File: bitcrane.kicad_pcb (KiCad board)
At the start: 4 copper layers, 110 x 100 mm, 87 parts, among them J1 PSU Comm, J14 0353180420, J15 0353180420, J16 0353180420, J17 0353180420, J2 Hashboard0, J3 0455580003, J4 61900411021, J5 61900411021, J6 61900411021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

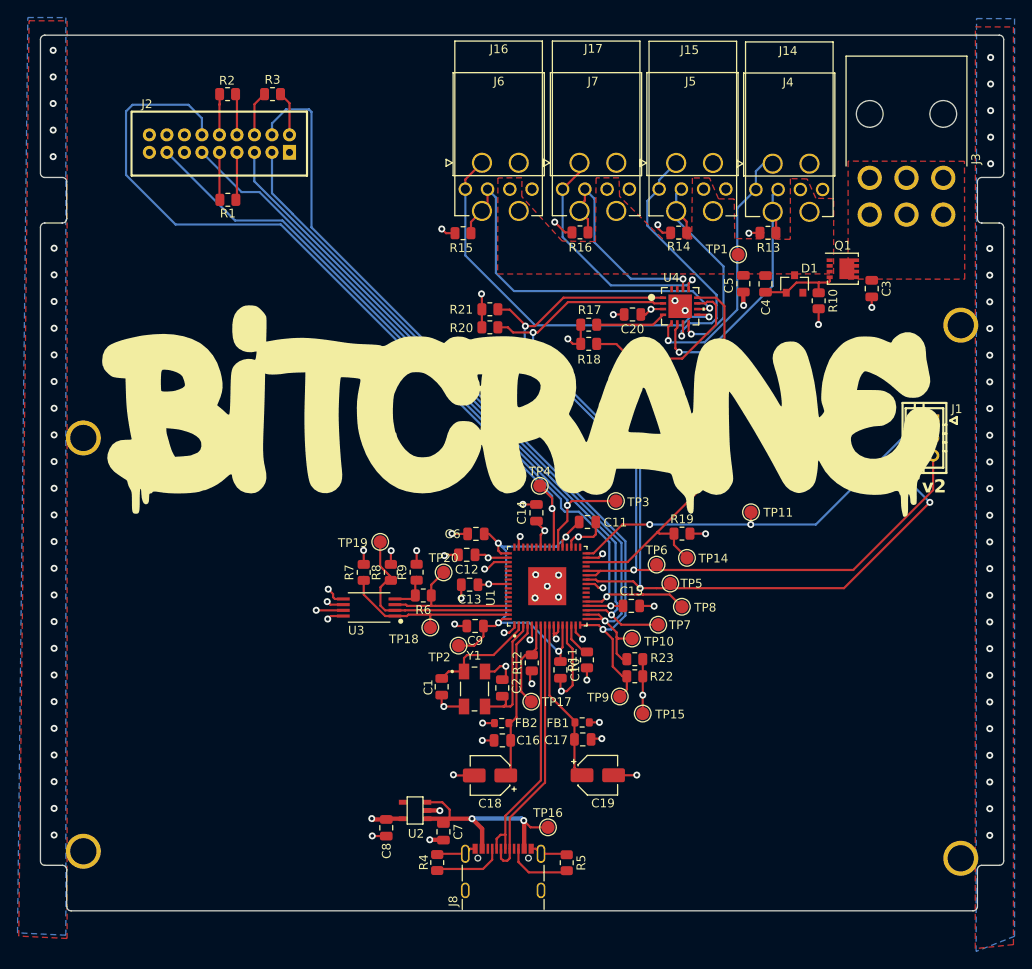
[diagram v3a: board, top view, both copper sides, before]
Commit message: switched to 3 HB connectors. added I2C hub. routed
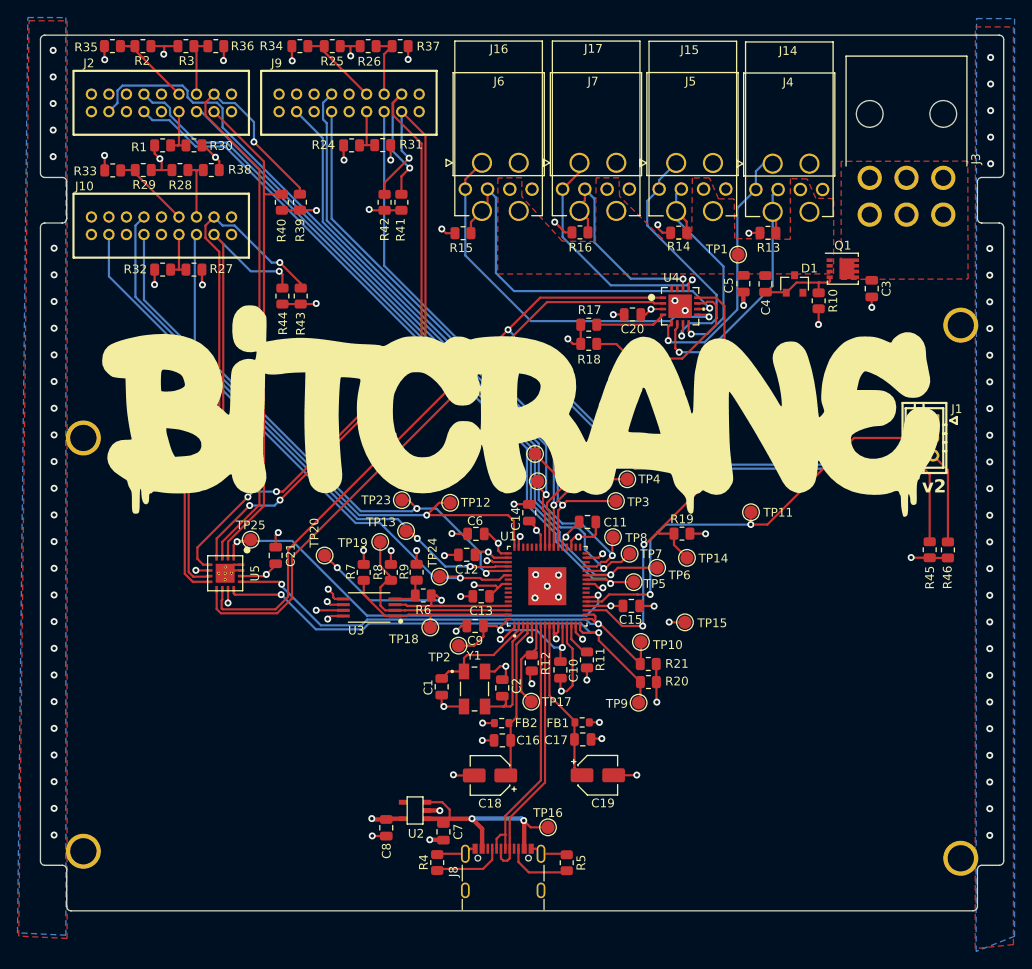
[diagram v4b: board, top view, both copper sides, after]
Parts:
- removed R22, R23: 4.7K, Resistor_SMD:R_0805_2012Metric
- added C21: 0.1uF, Capacitor_SMD:C_0805_2012Metric, F.Cu at (85.1, 93.7)
- added J10: Hashboard2, bitcart:CONN-TH_X2026WV-2-09D-46SN, F.Cu at (72.1, 56.0)
- added J9: Hashboard1, bitcart:CONN-TH_X2026WV-2-09D-46SN, F.Cu at (93.5, 42.0)
- added R24: 4.7K, Resistor_SMD:R_0805_2012Metric, F.Cu at (93.8, 46.8)
- added R25: 4.7K, Resistor_SMD:R_0805_2012Metric, F.Cu at (91.6, 35.5)
- added R26: 4.7K, Resistor_SMD:R_0805_2012Metric, F.Cu at (95.7, 35.5)
- added R27: 4.7K, Resistor_SMD:R_0805_2012Metric, F.Cu at (75.8, 61.0)
- added R28: 4.7K, Resistor_SMD:R_0805_2012Metric, F.Cu at (70.0, 49.6)
- added R29: 4.7K, Resistor_SMD:R_0805_2012Metric, F.Cu at (74.2, 49.6)
- added R30: 4.7K, Resistor_SMD:R_0805_2012Metric, F.Cu at (75.8, 46.8)
- added R31: 4.7K, Resistor_SMD:R_0805_2012Metric, F.Cu at (97.3, 46.8)
- added R32: 4.7K, Resistor_SMD:R_0805_2012Metric, F.Cu at (72.2, 61.0)
- added R33: 4.7K, Resistor_SMD:R_0805_2012Metric, F.Cu at (66.5, 49.7)
- added R34: 4.7K, Resistor_SMD:R_0805_2012Metric, F.Cu at (87.9, 35.5)
- added R35: 4.7K, Resistor_SMD:R_0805_2012Metric, F.Cu at (66.5, 35.5)
- added R36: 4.7K, Resistor_SMD:R_0805_2012Metric, F.Cu at (78.3, 35.5)
- added R37: 4.7K, Resistor_SMD:R_0805_2012Metric, F.Cu at (99.3, 35.5)
- added R38: 4.7K, Resistor_SMD:R_0805_2012Metric, F.Cu at (77.8, 49.6)
- added R39: 4.7K, Resistor_SMD:R_0805_2012Metric, F.Cu at (87.9, 53.3)
- added R40: 4.7K, Resistor_SMD:R_0805_2012Metric, F.Cu at (85.8, 53.3)
- added R41: 4.7K, Resistor_SMD:R_0805_2012Metric, F.Cu at (99.5, 53.3)
- added R42: 4.7K, Resistor_SMD:R_0805_2012Metric, F.Cu at (97.6, 53.3)
- added R43: 4.7K, Resistor_SMD:R_0805_2012Metric, F.Cu at (88.0, 64.0)
- added R44: 4.7K, Resistor_SMD:R_0805_2012Metric, F.Cu at (85.9, 64.0)
- added R45: 4.7K, Resistor_SMD:R_0805_2012Metric, F.Cu at (159.8, 93.0)
- added R46: 4.7K, Resistor_SMD:R_0805_2012Metric, F.Cu at (161.9, 93.0)
- added TP12: TestPoint, TestPoint:TestPoint_Pad_D1.5mm, F.Cu at (105.0, 87.7)
- added TP13: TestPoint, TestPoint:TestPoint_Pad_D1.5mm, F.Cu at (100.0, 90.9)
- added TP21: TestPoint, TestPoint:TestPoint_Pad_D1.5mm, F.Cu at (114.7, 82.1)
- added TP22: TestPoint, TestPoint:TestPoint_Pad_D1.5mm, F.Cu at (115.0, 85.2)
- added TP23: TestPoint, TestPoint:TestPoint_Pad_D1.5mm, F.Cu at (99.5, 87.3)
- added TP24: TestPoint, TestPoint:TestPoint_Pad_D1.5mm, F.Cu at (103.8, 96.1)
- added TP25: TestPoint, TestPoint:TestPoint_Pad_D1.5mm, F.Cu at (82.3, 91.9)
- added U5: PCA9546ARGVR, bitcart:QFN-16_EP_4x4_Pitch0.65mm, F.Cu at (79.4, 95.7)
- moved R20 44.4 mm to (127.7, 108.1), turned to 0 degrees
- moved R21 44.4 mm to (127.7, 106.1), turned to 0 degrees
- moved TP20 13.7 mm to (90.7, 93.7)
- moved TP15 11.5 mm to (131.9, 101.3)
- moved R3 11.3 mm to (74.9, 35.5), turned to 180 degrees
- moved TP8 11.2 mm to (123.7, 91.6)
- moved R2 11.1 mm to (70.0, 35.5), turned to 0 degrees
- moved TP4 10.0 mm to (125.3, 85.0)
- moved R1 9.71 mm to (72.2, 46.8)
- moved TP7 8.74 mm to (125.5, 93.5)
- moved J2 8.10 mm to (72.1, 42.0)
- moved TP5 4.18 mm to (126.0, 96.7)
- moved TP9 2.26 mm to (126.6, 110.5)
- moved C13 1.87 mm to (108.6, 98.3)
- moved TP10 1.08 mm to (126.8, 103.5)
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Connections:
- net /A0 renamed /A00
- net /A1 renamed /A10
- net /A2 renamed /A20
- J1 pad 3: /SDA -> /SDA3
- J1 pad 6: /SCL -> /SCL3
- J2 pad 11: /TXD -> /TXD0
- J2 pad 12: /RXD -> /RXD0
- J2 pad 15: /RST -> /RST0
- J2 pad 3: /HB_SDA -> /SDA0
- J2 pad 4: /HB_SCL -> /SCL0
- J2 pad 5: /PLUG -> /PLUG0
- TP10 pad 1: /HB_SDA -> /SDA
- TP3 pad 1: /TXD -> /TXD1
- TP4 pad 1: /RXD -> /RXD1
- TP5 pad 1: /SCL -> /TXD0
- TP6 pad 1: /SDA -> /RXD0
- TP7 pad 1: /PLUG -> /PLUG0
- TP8 pad 1: /RST -> /RST0
- TP9 pad 1: /HB_SCL -> /SCL
- U1 pad 16: /HB_SCL -> /SCL
- U1 pad 17: /HB_SDA -> /SDA
- U1 pad 18: /HB_SDA -> /SDA
- U1 pad 19: /PLUG -> /FAN_ALERT
- U1 pad 21: /RST -> /PSU_EN
- U1 pad 22: unconnected-(U1-ADBUS5-Pad22) -> /RESET
- U1 pad 26: /SCL -> /TXD0
- U1 pad 27: /SDA -> /RXD0
- U1 pad 28: /SDA -> /PLUG0
- U1 pad 29: unconnected-(U1-BDBUS3-Pad29) -> /RST0
- U1 pad 30: /FAN_ALERT -> unconnected-(U1-BDBUS4-Pad30)
- U1 pad 32: /PSU_EN -> unconnected-(U1-BDBUS5-Pad32)
- U1 pad 38: /TXD -> /TXD1
- U1 pad 39: /RXD -> /RXD1
- U1 pad 40: unconnected-(U1-CDBUS2-Pad40) -> /PLUG1
- U1 pad 41: unconnected-(U1-CDBUS3-Pad41) -> /RST1
- U1 pad 48: unconnected-(U1-DDBUS0-Pad48) -> /TXD2
- U1 pad 52: unconnected-(U1-DDBUS1-Pad52) -> /RXD2
- U1 pad 53: unconnected-(U1-DDBUS2-Pad53) -> /PLUG2
- U1 pad 54: unconnected-(U1-DDBUS3-Pad54) -> /RST2
- U4 pad 1: /SDA -> /SCL3
- U4 pad 2: /SCL -> /SDA3
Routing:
- net /SDA3: track 0.00 -> 136.8 mm, vias 0 -> 1
- net /SCL3: track 0.00 -> 134.9 mm, vias 0 -> 1
- net /HB_SCL: track 94.4 -> 0.00 mm, vias 1 -> 0
- net /RST0: track 0.00 -> 93.0 mm, vias 0 -> 1
- net /RXD: track 91.7 -> 0.00 mm, vias 1 -> 0
- net /RXD0: track 0.00 -> 89.3 mm, vias 0 -> 1
- net /RST: track 87.8 -> 0.00 mm, vias 1 -> 0
- net /TXD0: track 0.00 -> 85.6 mm, vias 0 -> 1
- net /HB_SDA: track 83.7 -> 0.00 mm, vias 1 -> 0
- net /SCL1: track 0.00 -> 82.1 mm, vias 0 -> 3
- net /PLUG: track 79.2 -> 0.00 mm, vias 1 -> 0
- net /PLUG0: track 0.00 -> 78.7 mm, vias 0 -> 1
- net /SDA1: track 0.00 -> 74.5 mm, vias 0 -> 3
- net /SCL0: track 0.00 -> 73.9 mm, vias 0 -> 1
- net /RXD1: track 0.00 -> 72.7 mm, vias 0 -> 1
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
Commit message: ran DRC, fixed errors, generated gerbers, generated BOM
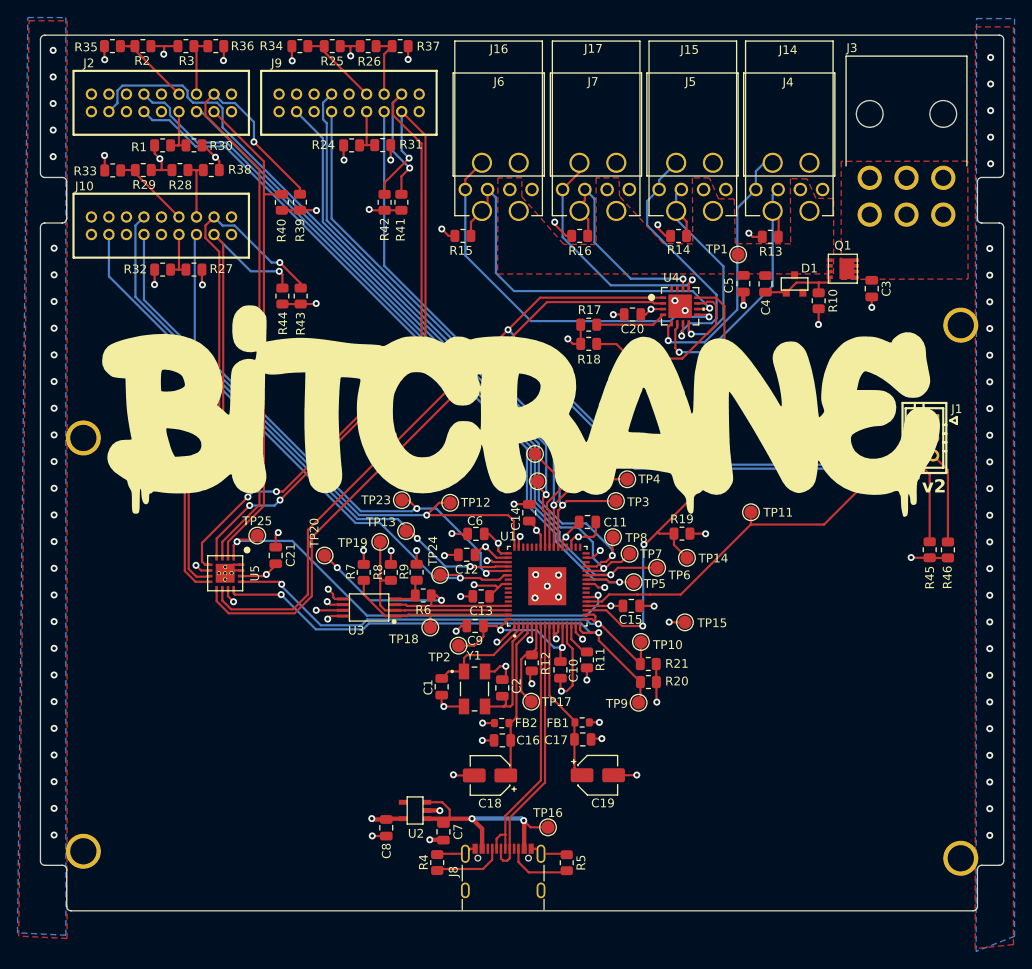
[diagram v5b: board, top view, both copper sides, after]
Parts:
- moved TP25 0.89 mm to (83.0, 91.4)
- moved R13 0.52 mm to (141.6, 57.3)
- moved R16 0.40 mm to (119.8, 57.2)
- moved R14 0.38 mm to (131.1, 57.2)
- moved R15 0.31 mm to (106.5, 57.2)
- moved TP24 0.20 mm to (103.9, 95.9)
- moved J14 0.10 mm to (141.9, 48.8)
- moved J5 0.05 mm to (136.5, 51.9)
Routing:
- net /PSU_EN: track 50.4 -> 46.8 mm, vias 2 -> 0
- net Net-(J14-Pin_4): track 31.6 -> 30.6 mm
- net VCCIO: track 94.6 -> 95.5 mm
- net /RESET: track 51.5 -> 52.4 mm
- net /TXD0: track 85.6 -> 86.4 mm
- net GND: track 106.3 -> 107.1 mm
- net /SDA3: track 136.8 -> 137.4 mm
- net Net-(J14-Pin_3): track 31.2 -> 31.8 mm
- net /SCL1: track 82.1 -> 81.5 mm
- net /SCL3: track 134.9 -> 135.4 mm
